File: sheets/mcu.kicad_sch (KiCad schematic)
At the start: 0 parts

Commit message: sch: RP2040 control plane + GPIO map
RP2040 (U24) core: W25Q128JVS QSPI flash, 12MHz crystal, RUN/BOOTSEL,
USB debug PHY (27.4R series), SWD, full 30-pin GPIO map per spec Sec.7.2.
I2C bus (2x TMP112 + Qwiic) pulled to +3V3_MCU, not +3V3, so an unpowered
RP2040 domain can't be back-fed through its own (non-failsafe) GPIOs.
LED-kill reworked high-side (Q33 DMG3415U-7 P-FET): SW2 slide switch and
GP9/LED_EN_CTL are independent kills, resistor values chosen so SW2 always
wins even if firmware fights it. RGB (SK6805-EC15, new custom symbol) runs
off the killable LED_PWR rail. POE_STS_RAW global label added to
power_input.kicad_sch (N_BTSTAT node) + divider on this sheet; GPIO
binding is BLOCKED (brief's GP0-29 map has no free slot) and left
unconnected pending a human decision -- see task-9-report.md.

0 errors / 600 ERC warnings (was 512), all checks pass.

Co-Authored-By: Claude Fable 5 <noreply@anthropic.com>
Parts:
- added C65, C66, C67, C68, C69, C70, C72, C75, C76, C77: 100nF, Capacitor_SMD:C_0402_1005Metric, symbol Device:C_Small
- added C71: 1uF, Capacitor_SMD:C_0603_1608Metric, symbol Device:C_Small
- added C73, C74: 27pF, Capacitor_SMD:C_0402_1005Metric, symbol Device:C_Small
- added D26: 1N4148W, Diode_SMD:D_SOD-323, symbol Device:D_Small
- added J4: SWD, Connector_PinHeader_2.54mm:PinHeader_1x03_P2.54mm_Vertical, symbol Connector_Generic:Conn_01x03
- added J5: Qwiic, Connector_JST:JST_SH_SM04B-SRSS-TB_1x04-1MP_P1.00mm, symbol Connector_Generic:Conn_01x04
- added J6: Fan, Connector_PinHeader_2.54mm:PinHeader_1x02_P2.54mm_Vertical, symbol Connector_Generic:Conn_01x02
- added J7: Spare, Connector_PinHeader_2.54mm:PinHeader_1x05_P2.54mm_Vertical, symbol Connector_Generic:Conn_01x05
- added Q33: DMG3415U-7, Package_TO_SOT_SMD:SOT-23, symbol sierra-to-usb:DMG3415U
- added Q34: 2N7002, Package_TO_SOT_SMD:SOT-23, symbol Transistor_FET:2N7002
- added R76: 1.0k, Resistor_SMD:R_0402_1005Metric, symbol Device:R_Small
- added R77: 10.0k, Resistor_SMD:R_0402_1005Metric, symbol Device:R_Small
- added R78, R79: 27.4, Resistor_SMD:R_0402_1005Metric, symbol Device:R_Small
- added R80, R81: 4.7k, Resistor_SMD:R_0603_1608Metric, symbol Device:R_Small
- added R82, R85, R87, R88, R89, R90, R91: 100k, Resistor_SMD:R_0603_1608Metric, symbol Device:R_Small
- added R83: 1.0k, Resistor_SMD:R_0603_1608Metric, symbol Device:R_Small
- added R84: 10.0k, Resistor_SMD:R_0603_1608Metric, symbol Device:R_Small
- added R86: 22k, Resistor_SMD:R_0603_1608Metric, symbol Device:R_Small
- added SW1: DIP-4, Button_Switch_THT:SW_DIP_x04, symbol Switch:SW_DIP_x04
- added SW2: LED_KILL, Button_Switch_THT:SW_SPDT_PCM12, symbol Switch:SW_SPDT
- added SW3: BOOTSEL, Button_Switch_SMD:SW_SPST_B3U-1000P, symbol Switch:SW_Push
- added SW4: RUN, Button_Switch_SMD:SW_SPST_B3U-1000P, symbol Switch:SW_Push
- added U24: RP2040, Package_DFN_QFN:QFN-56-1EP_7x7mm_P0.4mm_EP3.2x3.2mm, symbol MCU_RaspberryPi:RP2040
- added U25: W25Q128JVS, Package_SO:SOIC-8_5.3x5.3mm_P1.27mm, symbol Memory_Flash:W25Q128JVS
- added U26, U27: TMP112AIDRLR, Package_TO_SOT_SMD:SOT-563, symbol Sensor_Temperature:TMP112xxDRL
- added U28: SK6805-EC15, LED_SMD:LED_SK6805-EC15_1.5x1.5mm, symbol sierra-to-usb:SK6805-EC15
- added Y1: 12MHz, Crystal:Crystal_SMD_3225-4Pin_3.2x2.5mm, symbol Device:Crystal_GND24
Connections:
- new net +12V: D26.1 (K), J6.1 (Pin_1)
- new net +3V3: Q33.2 (S), R83.2
- new net +3V3_MCU: C65.1, C66.1, C68.1, C69.1, C70.1, C72.1, C75.1, C76.1, J5.2 (Pin_2), J7.4 (Pin_4), R77.2, R80.2, R81.2, R88.2, R89.2, R90.2, R91.2, U24.1 (IOVDD), U24.10 (IOVDD), U24.22 (IOVDD), U24.33 (IOVDD), U24.42 (IOVDD), U24.43 (ADC_AVDD), U24.44 (VREG_VIN), U24.48 (USB_VDD), U24.49 (IOVDD), U25.8 (VCC), U26.5 (V+), U27.4 (ADD0), U27.5 (V+)
- new net CLKREQ_N: U24.30 (GPIO19)
- new net DIP0: R88.1, SW1.1, U24.31 (GPIO20)
- new net DIP1: R89.1, SW1.2, U24.32 (GPIO21)
- new net DIP2: R90.1, SW1.3, U24.34 (GPIO22)
- new net DIP3: R91.1, SW1.4, U24.35 (GPIO23)
- new net DVDD_1V1: C67.1, C71.1, U24.23 (DVDD), U24.45 (VREG_VOUT), U24.50 (DVDD)
- new net FAN_PWM: Q34.1 (G), R87.1, U24.18 (GPIO15)
- new net FCPO_CTL: U24.6 (GPIO4)
- new net GND: C65.2, C66.2, C67.2, C68.2, C69.2, C70.2, C71.2, C72.2, C73.2, C74.2, C75.2, C76.2, C77.2, J4.3 (Pin_3), J5.1 (Pin_1), J7.5 (Pin_5), Q34.2 (S), R82.2, R86.2, R87.2, SW1.5, SW1.6, SW1.7, SW1.8, SW3.2, SW4.2, U24.19 (TESTEN), U24.57 (GND), U25.4 (GND), U26.2 (GND), U26.4 (ADD0), U27.2 (GND), U28.4 (GND), Y1.2 (G), Y1.4 (G)
- new net I2C_SCL: J5.4 (Pin_4), R81.1, U24.3 (GPIO1), U26.1 (SCL), U27.1 (SCL)
- new net I2C_SDA: J5.3 (Pin_3), R80.1, U24.2 (GPIO0), U26.6 (SDA), U27.6 (SDA)
- new net LED_EN_CTL: R84.2, U24.12 (GPIO9)
- new net LED_PWR: C77.1, Q33.3 (D), U28.2 (VDD)
- new net MCU_GPIO24: J7.1 (Pin_1), U24.36 (GPIO24)
- new net MCU_GPIO25: J7.2 (Pin_2), U24.37 (GPIO25)
- new net MCU_GPIO29: J7.3 (Pin_3), U24.41 (GPIO29/ADC3)
- new net MCU_SWCLK: J4.1 (Pin_1), U24.24 (SWCLK)
- new net MCU_SWDIO: J4.2 (Pin_2), U24.25 (SWDIO)
- new net MCU_USB_DM: R79.1, U24.46 (USB_DM)
- new net MCU_USB_DP: R78.1, U24.47 (USB_DP)
- new net MRST_CTL: U24.9 (GPIO7)
- new net MUX_USB2_SEL: U24.13 (GPIO10)
- new net N_FAN_RTN: D26.2 (A), J6.2 (Pin_2), Q34.3 (D)
- new net N_LEDKILL_GATE: Q33.1 (G), R82.1, R84.1, SW2.2 (B)
- new net N_SW2_KILL: R83.1, SW2.1 (A)
- new net PCIE_DIS_CTL: U24.7 (GPIO5)
- new net PERST_N: U24.29 (GPIO18)
- new net POE_STATUS: R85.2, R86.1
- new net POE_STS_RAW: R85.1
- new net QSPI_SCLK: U24.52 (QSPI_SCLK), U25.6 (CLK)
- new net QSPI_SD0: U24.53 (QSPI_SD0), U25.5 (DI/IO_{0})
- new net QSPI_SD1: U24.55 (QSPI_SD1), U25.2 (DO/IO_{1})
- new net QSPI_SD2: U24.54 (QSPI_SD2), U25.3 (~{WP}/IO_{2})
- new net QSPI_SD3: U24.51 (QSPI_SD3), U25.7 (~{HOLD}/~{RESET}/IO_{3})
- new net QSPI_SS: SW3.1, U24.56 (~{QSPI_SS}), U25.1 (~{CS})
- new net RGB_DI: U24.17 (GPIO14), U28.1 (DIN)
- new net RP2040_RUN: R77.1, SW4.1, U24.26 (RUN)
- new net RTL_RST_N: U24.15 (GPIO12)
- new net SIM_SEL: U24.14 (GPIO11)
- new net UIM2_DET_CTL: U24.16 (GPIO13)
- new net USB2_MCU_DM: U24.5 (GPIO3)
- new net USB2_MCU_DP: U24.4 (GPIO2)
- new net USB_DBG_DM: R79.2
- new net USB_DBG_DP: R78.2
- new net VBUSSNS_CTL: U24.11 (GPIO8)
- new net VMON_12V: U24.38 (GPIO26/ADC0)
- new net VMON_1V8: U24.40 (GPIO28/ADC2)
- new net VMON_3V3: U24.39 (GPIO27/ADC1)
- new net WAKE_N: U24.28 (GPIO17)
- new net WDIS_CTL: U24.8 (GPIO6)
- new net WWAN_LED_N: U24.27 (GPIO16)
- new net XTAL1: C73.1, R76.2, Y1.1
- new net XTAL_XIN: R76.1, U24.20 (XIN)
- new net XTAL_XOUT: C74.1, U24.21 (XOUT), Y1.3
- no-connect marks 0 -> 4
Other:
- note added: "J_FAN pinout: 1=+12V, 2=switched return (Q34 low-side, 2-wire fan; PWM'd via FAN_PWM, no separate PWM wire to fan). D26 flyback across the switched leg."
- note added: "J_QWIIC pinout: SparkFun Qwiic standard = 1 GND, 2 +3V3, 3 SDA, 4 SCL (JST SH 1mm 4-pin). Powered from +3V3_MCU to match the I2C pull-up domain (see report)."
- note added: "J_SWD pinout: 1=SWCLK 2=SWDIO 3=GND (3-pin tag-connect style debug header)"
- note added: "J_spare (J18): 1=GP24 2=GP25 3=GP29(ADC3) 4=+3V3_MCU 5=GND."
- note added: "LED-kill gate logic (high-side, amendment 1): default (SW2 idle + GP9 released) -> R84 100k pulldown -> gate=0V -> Q33 ON -> LED_PWR=+3V3 (LEDs on). SW2 engaged (throw A) OR GP9 driven HIGH -> gate pulled toward +3V3 through 1k (SW2) or 10k (GP9) -> |Vgs| << DMG3415U-7 threshold -> Q33 OFF -> LEDs dark. R83=1k dominates R84/R85 even if GP9 is simultaneously driven LOW (worst-case conflict still y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"
- note added: "POE_STATUS divider (amendment 2): POE_STS_RAW (0-11V, from power_input N_BTSTAT) -100k-> POE_STATUS -22k-> GND. 11V*22k/122k=1.98V (also fine at 0V). BLOCKED: brief's own GP0-GP29 map is FULLY populated (30/30, incl. 3 J18 spares) with no POE_STATUS slot -- per task instructions ("any pin conflict: STOP, do not shuffle silently") this net is NOT bound to an RP2040 pin here. Recommend GP29 (spare-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"
- note added: "RGB (amendment 5): powered from LED_PWR (killable 3.3V rail), not +3V3_MCU -- SK6805-EC15 VDD floor is 3.7V (below-datasheet-floor 3.3V op is sourcing.md-flagged standard practice). VIH arithmetic: VIH ~= 0.7*VDD_actual = 0.7*3.3V = 2.31V; RGB_DI driven from a 3.3V RP2040 GPIO satisfies VIH with 0.99V margin (43%)."
- note added: "RP2040 GPIO map per spec Sec.7.2 (binding interface, firmware plan consumes verbatim). GP2/GP3 adjacent for pico-pio-usb. GP16 WWAN_LED_N: no external pull -- firmware enables the RP2040 internal pull-up; released-pin level approx 1.3-1.7V < RP2040 VIH."
- note added: "SW1 DIP-4 -> DIP0-3, 100k pull-ups to +3V3_MCU, closed=low (brief Step-1: SW1.1=DIP0)."
- note added: "U26 TMP112 (0x48, ADD0->GND) -- placed near CN1 (M.2 socket) for module-adjacent thermal sensing."
- note added: "U27 TMP112 (0x49, ADD0->+3V3_MCU) -- placed near U3/U10 (buck + PoE PD) for power-stage thermal sensing."

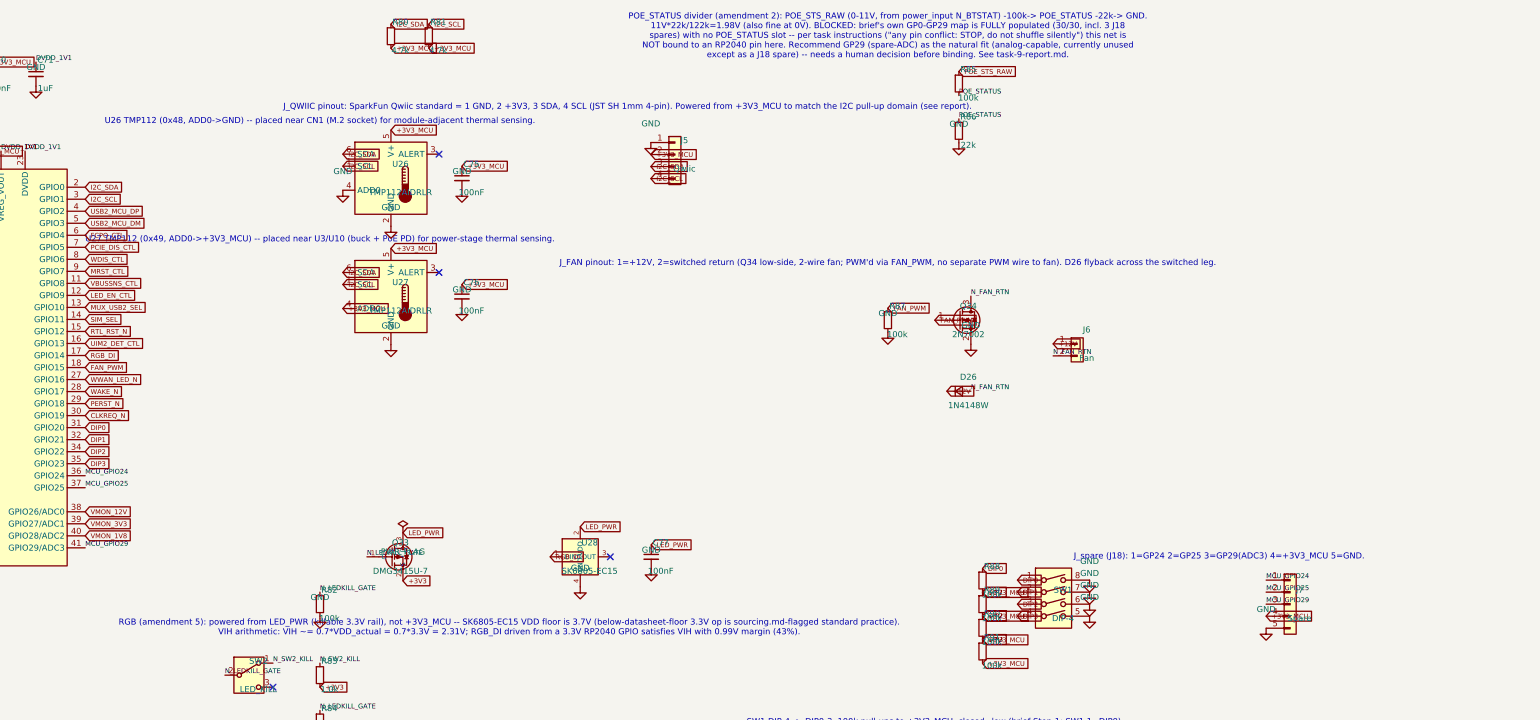
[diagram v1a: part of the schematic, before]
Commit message: sch: mcu — POE_STATUS to GP29 per controller resolution
GP29/ADC3 (previously a J18 spare) now reads the PoE status divider
(0-1.98V analog). J7 spare header shrinks 5->4 pins (GP24/GP25 +
3V3_MCU/GND). Netchecks pin U24.GPIO29/ADC3 = POE_STATUS and the new J7
pinout; checker all-pass, ERC still 0 errors / 600 warnings.

Co-Authored-By: Claude Fable 5 <noreply@anthropic.com>
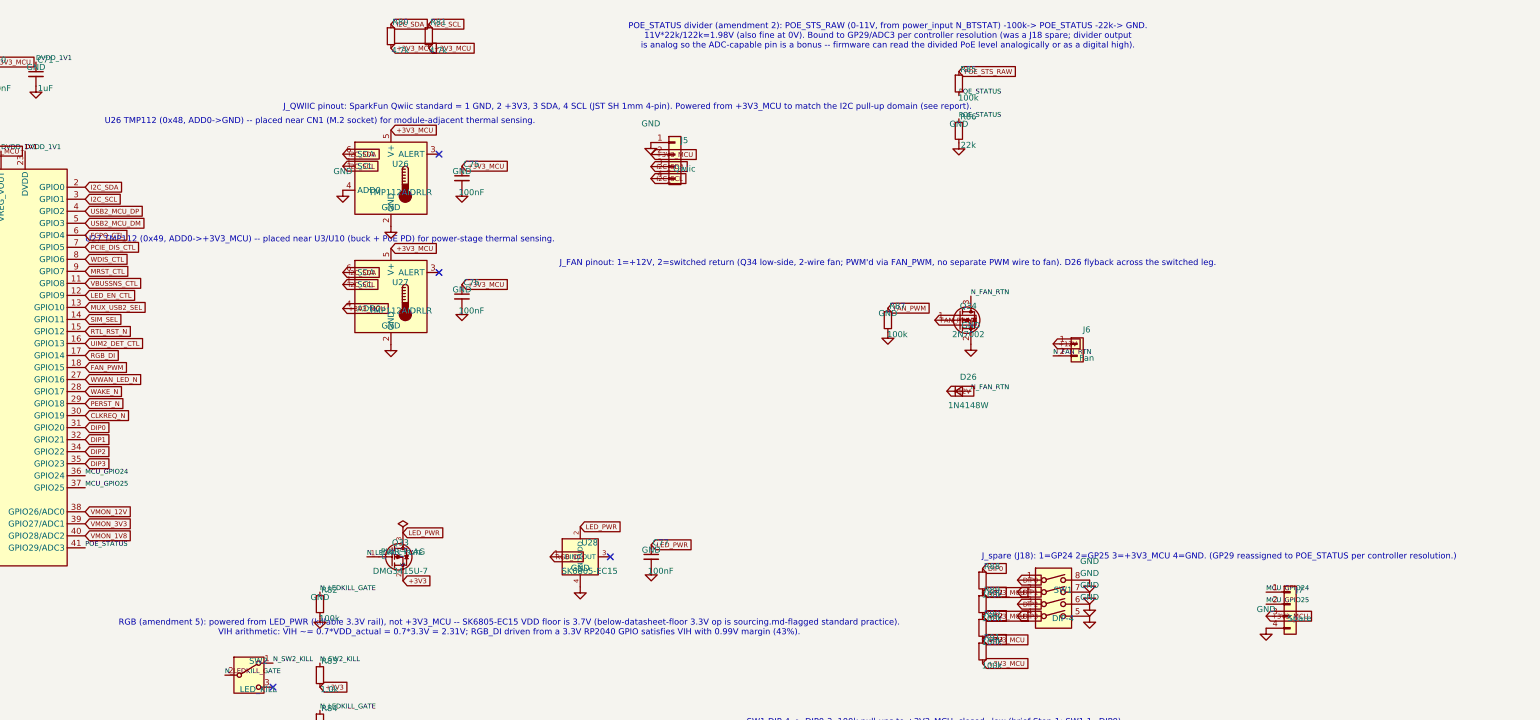
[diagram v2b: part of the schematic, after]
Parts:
- removed J7: Spare, Connector_PinHeader_2.54mm:PinHeader_1x05_P2.54mm_Vertical, symbol Connector_Generic:Conn_01x05
- added J7: Spare, Connector_PinHeader_2.54mm:PinHeader_1x04_P2.54mm_Vertical, symbol Connector_Generic:Conn_01x04
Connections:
- net MCU_GPIO29 is gone; now on net POE_STATUS: U24.41 (GPIO29/ADC3)
- net +3V3_MCU: now also J7.3 (Pin_3)
- net GND: now also J7.4 (Pin_4)
- net MCU_GPIO24: now also J7.1 (Pin_1)
- net MCU_GPIO25: now also J7.2 (Pin_2)
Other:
- note added: "J_spare (J18): 1=GP24 2=GP25 3=+3V3_MCU 4=GND. (GP29 reassigned to POE_STATUS per controller resolution.)"
- note added: "POE_STATUS divider (amendment 2): POE_STS_RAW (0-11V, from power_input N_BTSTAT) -100k-> POE_STATUS -22k-> GND. 11V*22k/122k=1.98V (also fine at 0V). Bound to GP29/ADC3 per controller resolution (was a J18 spare; divider output is analog so the ADC-capable pin is a bonus -- firmware can read the divided PoE level analogically or as a digital high)."
- note removed: "J_spare (J18): 1=GP24 2=GP25 3=GP29(ADC3) 4=+3V3_MCU 5=GND."
- note removed: "POE_STATUS divider (amendment 2): POE_STS_RAW (0-11V, from power_input N_BTSTAT) -100k-> POE_STATUS -22k-> GND. 11V*22k/122k=1.98V (also fine at 0V). BLOCKED: brief's own GP0-GP29 map is FULLY populated (30/30, incl. 3 J18 spares) with no POE_STATUS slot -- per task instructions ("any pin conflict: STOP, do not shuffle silently") this net is NOT bound to an RP2040 pin here. Recommend GP29 (spare-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"
